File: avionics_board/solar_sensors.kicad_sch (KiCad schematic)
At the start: 5 parts, among them U15 TCA9548APWR, U16 TCA9548APWR

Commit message: add headers for ACS and sun sensors
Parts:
- removed C54: 100nF, Capacitor_SMD:C_0402_1005Metric_Pad0.74x0.62mm_HandSolder, symbol Device:C
- removed R41: 100K, Resistor_SMD:R_0402_1005Metric_Pad0.72x0.64mm_HandSolder, symbol Device:R
- removed U16: TCA9548APWR, Package_SO:TSSOP-24_4.4x7.8mm_P0.65mm, symbol Interface_Expansion:TCA9548APWR
- added RN1, RN2: EXBA10P472J, Common:C_ARRAY_EXBA_PAN, symbol Common:EXBA10P472J
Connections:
- net VIN: now also RN1.10, RN1.5, RN2.10, RN2.5
- net Solar Sensors XP/SCL0 renamed SC0
- net SC0: now also RN1.9
- net Solar Sensors XP/SCL1 renamed SC1
- net SC1: now also RN1.8
- net Solar Sensors XP/SDA0 renamed SD0
- net SD0: now also RN1.1
- net Solar Sensors XP/SDA1 renamed SD1
- net SD1: now also RN1.2
- net Solar Sensor TLS1/SCL0 renamed SC2
- net SC2: now also RN1.7
- net Solar Sensor TLS1/SCL1 renamed SC3
- net SC3: now also RN1.6
- net Solar Sensor TLS1/SDA0 renamed SD2
- net SD2: now also RN1.3
- net Solar Sensor TLS1/SDA1 renamed SD3
- net SD3: now also RN1.4
- net Solar Sensor TLS2/SCL0 renamed SC4
- net SC4: now also RN2.9
- net Solar Sensor TLS2/SCL1 renamed SC5
- net SC5: now also RN2.8
- net Solar Sensor TLS2/SDA0 renamed SD4
- net SD4: now also RN2.1
- net Solar Sensor TLS2/SDA1 renamed SD5
- net SD5: now also RN2.2
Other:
- sheet Solar Sensor TLS0 renamed Solar Sensors XP
- removed sheet Solar Sensor TLS1
- removed sheet Solar Sensor TLS2
- removed sheet Solar Sensor TLS3
- removed sheet Solar Sensor TLS4
- removed sheet Solar Sensor TLS5
- added sheet Solar Sensors XN (solar_sensor_tls.kicad_sch)
- added sheet Solar Sensors YN (solar_sensor_tls.kicad_sch)
- added sheet Solar Sensors YP (solar_sensor_tls.kicad_sch)
- added sheet Solar Sensors ZN (solar_sensor_tls.kicad_sch)
- added sheet Solar Sensors ZP (solar_sensor_tls.kicad_sch)
- sheet Solar Sensors XP ports: added *INT, SCL, SDA; removed *INT0, *INT1, SCL0, SCL1, SDA0, SDA1
- note removed: "+ Sides"
- note removed: "- Sides"

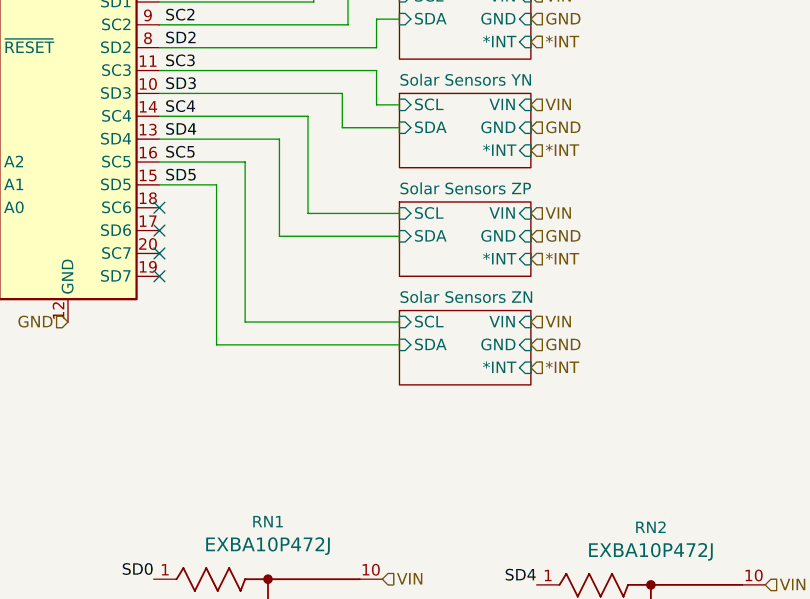
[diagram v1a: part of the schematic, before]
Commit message: use SAMTEC connectors for AVI to side panels, try HARWIN ones next
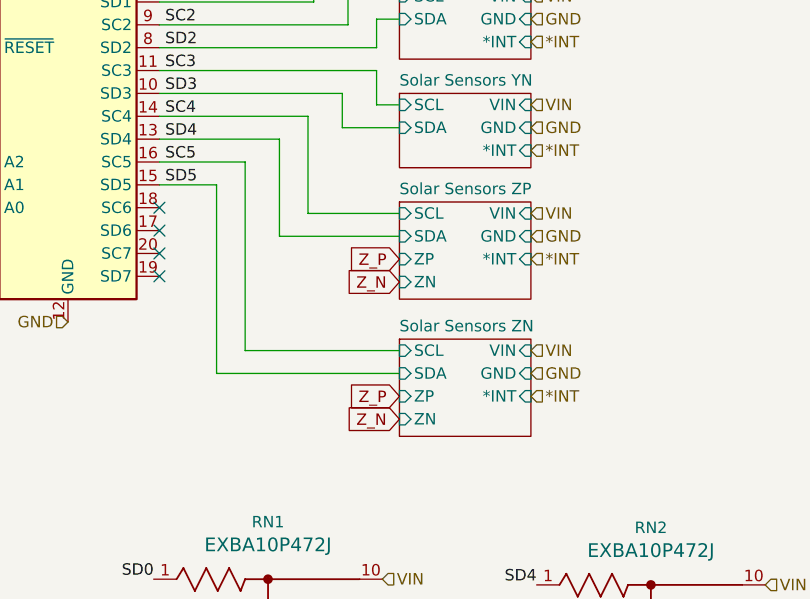
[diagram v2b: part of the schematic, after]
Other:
- sheet Solar Sensors XN: file solar_sensor_tls.kicad_sch -> solar_sensor_xy.kicad_sch
- sheet Solar Sensors XP: file solar_sensor_tls.kicad_sch -> solar_sensor_xy.kicad_sch
- sheet Solar Sensors YN: file solar_sensor_tls.kicad_sch -> solar_sensor_xy.kicad_sch
- sheet Solar Sensors YP: file solar_sensor_tls.kicad_sch -> solar_sensor_xy.kicad_sch
- sheet Solar Sensors ZN: file solar_sensor_tls.kicad_sch -> solar_sensor_z.kicad_sch
- sheet Solar Sensors ZN ports: added ZN, ZP; removed none
- sheet Solar Sensors ZP: file solar_sensor_tls.kicad_sch -> solar_sensor_z.kicad_sch
- sheet Solar Sensors ZP ports: added ZN, ZP; removed none
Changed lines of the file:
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@@
 	(wire
 		(pts
-			(xy 104.775 95.885) (xy 104.775 113.665)
+			(xy 104.775 95.885) (xy 104.775 116.84)
 		)
 		(stroke
@@
 	(wire
 		(pts
-			(xy 101.6 116.205) (xy 121.92 116.205)
+			(xy 101.6 119.38) (xy 121.92 119.38)
 		)
 		(stroke
@@
 	(wire
 		(pts
-			(xy 101.6 98.425) (xy 101.6 116.205)
+			(xy 101.6 98.425) (xy 101.6 119.38)
 		)
 		(stroke
@@
 	(wire
 		(pts
-			(xy 104.775 113.665) (xy 121.92 113.665)
+			(xy 104.775 116.84) (xy 121.92 116.84)
 		)
 		(stroke
@@
 		)
 	)
+	(global_label "Z_P"
+		(shape input)
+		(at 121.92 121.92 180)
+		(fields_autoplaced yes)
+		(effects
+			(font
+				(size 1.27 1.27)
+			)
+			(justify right)
+		)
+		(property "Intersheetrefs" "${INTERSHEET_REFS}"
+			(at 115.4877 121.92 0)
+			(effects
+				(font
+					(size 1.27 1.27)
+				)
+				(justify right)
+				(hide yes)
+			)
+		)
+	)
+	(global_label "Z_N"
+		(shape input)
+		(at 121.92 109.22 180)
+		(fields_autoplaced yes)
+		(effects
+			(font
+				(size 1.27 1.27)
+			)
+			(justify right)
+		)
+		(property "Intersheetrefs" "${INTERSHEET_REFS}"
+			(at 115.4272 109.22 0)
+			(effects
+				(font
+					(size 1.27 1.27)
+				)
+				(justify right)
+				(hide yes)
+			)
+		)
+	)
+	(global_label "Z_P"
+		(shape input)
+		(at 121.92 106.68 180)
+		(fields_autoplaced yes)
+		(effects
+			(font
+				(size 1.27 1.27)
+			)
+			(justify right)
+		)
+		(property "Intersheetrefs" "${INTERSHEET_REFS}"
+			(at 115.4877 106.68 0)
+			(effects
+				(font
+					(size 1.27 1.27)
+				)
+				(justify right)
+				(hide yes)
+			)
+		)
+	)
+	(global_label "Z_N"
+		(shape input)
+		(at 121.92 124.46 180)
+		(fields_autoplaced yes)
+		(effects
+			(font
+				(size 1.27 1.27)
+			)
+			(justify right)
+		)
+		(property "Intersheetrefs" "${INTERSHEET_REFS}"
+			(at 115.4272 124.46 0)
+			(effects
+				(font
+					(size 1.27 1.27)
+				)
+				(justify right)
+				(hide yes)
+			)
+		)
+	)
 	(hierarchical_label "*INT"
 		(shape input)
@@
 	(hierarchical_label "GND"
 		(shape input)
-		(at 136.525 116.205 0)
+		(at 136.525 119.38 0)
 		(fields_autoplaced yes)
 		(effects
@@
 	(hierarchical_label "VIN"
 		(shape input)
-		(at 136.525 113.665 0)
+		(at 136.525 116.84 0)
 		(fields_autoplaced yes)
 		(effects
@@
 	(hierarchical_label "*INT"
 		(shape input)
-		(at 136.525 118.745 0)
+		(at 136.525 121.92 0)
 		(fields_autoplaced yes)
 		(effects
@@
 			)
 		)
-		(property "Sheetfile" "solar_sensor_tls.kicad_sch"
+		(property "Sheetfile" "solar_sensor_xy.kicad_sch"
 			(at 121.92 97.1046 0)
 			(effects
@@
 	(sheet
 		(at 121.92 100.33)
-		(size 14.605 8.255)
+		(size 14.605 10.795)
 		(fields_autoplaced yes)
 		(stroke
@@
 			)
 		)
-		(property "Sheetfile" "solar_sensor_tls.kicad_sch"
-			(at 121.92 109.1696 0)
+		(property "Sheetfile" "solar_sensor_z.kicad_sch"
+			(at 121.92 111.7096 0)
 			(effects
 				(font
@@
 		(pin "SDA" input
 			(at 121.92 104.14 180)
+			(effects
+				(font
+					(size 1.27 1.27)
+				)
+				(justify left)
+			)
+		)
+		(pin "ZP" input
+			(at 121.92 106.68 180)
+			(effects
+				(font
+					(size 1.27 1.27)
+				)
+				(justify left)
+			)
+		)
+		(pin "ZN" input
+			(at 121.92 109.22 180)
 			(effects
 				(font
@@
 	)
 	(sheet
-		(at 121.92 112.395)
-		(size 14.605 8.255)
+		(at 121.92 115.57)
+		(size 14.605 10.795)
 		(fields_autoplaced yes)
 		(stroke
@@
 		)
 		(property "Sheetname" "Solar Sensors ZN"
-			(at 121.92 111.6834 0)
+			(at 121.92 114.8584 0)
 			(effects
 				(font
@@
 			)
 		)
-		(property "Sheetfile" "solar_sensor_tls.kicad_sch"
-			(at 121.92 121.2346 0)
+		(property "Sheetfile" "solar_sensor_z.kicad_sch"
+			(at 121.92 126.9496 0)
 			(effects
 				(font
@@
 		)
 		(pin "VIN" input
-			(at 136.525 113.665 0)
+			(at 136.525 116.84 0)
 			(effects
 				(font
@@
 		)
 		(pin "GND" input
-			(at 136.525 116.205 0)
+			(at 136.525 119.38 0)
 			(effects
 				(font
@@
 		)
 		(pin "SCL" input
-			(at 121.92 113.665 180)
+			(at 121.92 116.84 180)
 			(effects
 				(font
@@
 		)
 		(pin "*INT" input
-			(at 136.525 118.745 0)
+			(at 136.525 121.92 0)
 			(effects
 				(font
@@
 		)
 		(pin "SDA" input
-			(at 121.92 116.205 180)
+			(at 121.92 119.38 180)
+			(effects
+				(font
+					(size 1.27 1.27)
+				)
+				(justify left)
+			)
+		)
+		(pin "ZP" input
+			(at 121.92 121.92 180)
+			(effects
+				(font
+					(size 1.27 1.27)
+				)
+				(justify left)
+			)
+		)
+		(pin "ZN" input
+			(at 121.92 124.46 180)
 			(effects
 				(font
@@
 			)
 		)
-		(property "Sheetfile" "solar_sensor_tls.kicad_sch"
+		(property "Sheetfile" "solar_sensor_xy.kicad_sch"
 			(at 121.92 85.0396 0)
 			(effects
@@
 			)
 		)
-		(property "Sheetfile" "solar_sensor_tls.kicad_sch"
+		(property "Sheetfile" "solar_sensor_xy.kicad_sch"
 			(at 121.92 60.9096 0)
 			(effects
@@
 			)
 		)
-		(property "Sheetfile" "solar_sensor_tls.kicad_sch"
+		(property "Sheetfile" "solar_sensor_xy.kicad_sch"
 			(at 121.92 72.9746 0)
 			(effects

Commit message: AVI: using through hole M50 connectors for sun detectors and ACS
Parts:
- RN1, RN2: value EXBA10P472J -> 4K7; AVAILABILITY Warning -> (none); MF Yageo -> (none); MOUSER-PURCHASE-URL https://snapeda.com/shop?store=Mouser&id=600502 -> (none); MP YC158TJR-0722KL -> (none); Manufacturer (none) -> Panasonic; PACKAGE 1206 Yageo -> (none); PRICE None -> (none); Part Number (none) -> EXB-A10P472J; Tolerance (none) -> 5
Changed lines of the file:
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@@
 			)
 		)
-		(property "Value" "EXBA10P472J"
+		(property "Value" "4K7"
 			(at 107.3161 138.43 0)
 			(effects
@@
 			)
 		)
-		(property "Datasheet" "EXBA10P472J"
+		(property "Datasheet" "https://industrial.panasonic.com/ww/products/pt/resistor-network-array/models/EXBA10P472J"
 			(at 94.615 142.24 0)
 			(effects
@@
 			)
 		)
-		(property "MF" "Yageo"
+		(property "Manufacturer" "Panasonic"
 			(at 94.615 142.24 0)
 			(effects
@@
 					(size 1.27 1.27)
 				)
-				(justify bottom)
 				(hide yes)
 			)
 		)
-		(property "MOUSER-PURCHASE-URL" "https://snapeda.com/shop?store=Mouser&id=600502"
+		(property "Part Number" "EXB-A10P472J"
 			(at 94.615 142.24 0)
 			(effects
@@
 					(size 1.27 1.27)
 				)
-				(justify bottom)
 				(hide yes)
 			)
 		)
-		(property "PACKAGE" "1206 Yageo"
+		(property "Tolerance" "5"
 			(at 94.615 142.24 0)
 			(effects
@@
 					(size 1.27 1.27)
 				)
-				(justify bottom)
-				(hide yes)
-			)
-		)
-		(property "PRICE" "None"
-			(at 94.615 142.24 0)
-			(effects
-				(font
-					(size 1.27 1.27)
-				)
-				(justify bottom)
-				(hide yes)
-			)
-		)
-		(property "MP" "YC158TJR-0722KL"
-			(at 94.615 142.24 0)
-			(effects
-				(font
-					(size 1.27 1.27)
-				)
-				(justify bottom)
-				(hide yes)
-			)
-		)
-		(property "AVAILABILITY" "Warning"
-			(at 94.615 142.24 0)
-			(effects
-				(font
-					(size 1.27 1.27)
-				)
-				(justify bottom)
 				(hide yes)
 			)
@@
 			)
 		)
-		(property "Value" "EXBA10P472J"
+		(property "Value" "4K7"
 			(at 149.8611 139.065 0)
 			(effects
@@
 			)
 		)
-		(property "Datasheet" "EXBA10P472J"
+		(property "Datasheet" "https://industrial.panasonic.com/ww/products/pt/resistor-network-array/models/EXBA10P472J"
 			(at 137.16 142.875 0)
 			(effects
@@
 			)
 		)
-		(property "MF" "Yageo"
+		(property "Manufacturer" "Panasonic"
 			(at 137.16 142.875 0)
 			(effects
@@
 					(size 1.27 1.27)
 				)
-				(justify bottom)
 				(hide yes)
 			)
 		)
-		(property "MOUSER-PURCHASE-URL" "https://snapeda.com/shop?store=Mouser&id=600502"
+		(property "Part Number" "EXB-A10P472J"
 			(at 137.16 142.875 0)
 			(effects
@@
 					(size 1.27 1.27)
 				)
-				(justify bottom)
 				(hide yes)
 			)
 		)
-		(property "PACKAGE" "1206 Yageo"
+		(property "Tolerance" "5"
 			(at 137.16 142.875 0)
 			(effects
@@
 					(size 1.27 1.27)
 				)
-				(justify bottom)
 				(hide yes)
 			)
-		)
-		(property "PRICE" "None"
-			(at 137.16 142.875 0)
-			(effects
-				(font
-					(size 1.27 1.27)
-				)
-				(justify bottom)
-				(hide yes)
-			)
-		)
-		(property "MP" "YC158TJR-0722KL"
-			(at 137.16 142.875 0)
-			(effects
-				(font
-					(size 1.27 1.27)
-				)
-				(justify bottom)
-				(hide yes)
-			)
-		)
-		(property "AVAILABILITY" "Warning"
-			(at 137.16 142.875 0)
-			(effects
-				(font
-					(size 1.27 1.27)
-				)
-				(justify bottom)
-				(hide yes)
-			)

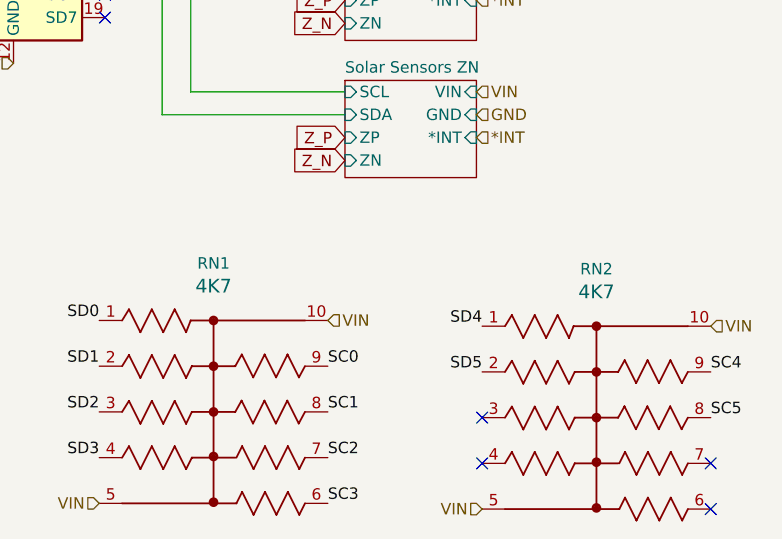
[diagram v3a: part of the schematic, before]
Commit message: QC, add second 3V regulator to AUX, INT pullups on AUX SCI AVI
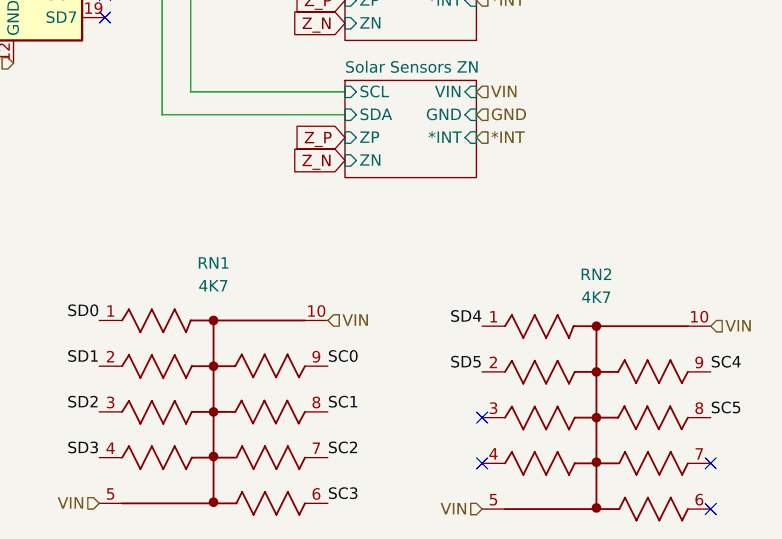
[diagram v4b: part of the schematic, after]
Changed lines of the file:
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@@
 			(effects
 				(font
-					(size 1.524 1.524)
+					(size 1.27 1.27)
 				)
 			)
@@
 		(fields_autoplaced yes)
 		(property "Reference" "RN2"
-			(at 149.8611 136.525 0)
+			(at 149.8611 137.16 0)
 			(effects
 				(font
@@
 		)
 		(property "Value" "4K7"
-			(at 149.8611 139.065 0)
+			(at 149.8611 139.7 0)
 			(effects
 				(font
-					(size 1.524 1.524)
+					(size 1.27 1.27)
 				)
 			)
